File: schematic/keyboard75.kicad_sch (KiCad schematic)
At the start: 389 parts, among them J1 SWD, J1 USB_C_Receptacle_USB2.0, J4 PTH, J5 PTH, K0_0 KEYSW, K0_1 KEYSW, K0_10 KEYSW, K0_11 KEYSW, K0_12 KEYSW, K0_13 KEYSW, K0_14 KEYSW, K0_15 KEYSW, K0_2 KEYSW, K0_3 KEYSW, K0_4 KEYSW, K0_5 KEYSW, K0_6 KEYSW, K0_7 KEYSW, K0_8 KEYSW, K0_9 KEYSW, K1_0 KEYSW, K1_1 KEYSW, K1_10 KEYSW, K1_11 KEYSW, K1_12 KEYSW, K1_13 KEYSW, K1_14 KEYSW, K1_2 KEYSW, K1_3 KEYSW, K1_4 KEYSW, K1_5 KEYSW, K1_6 KEYSW, K1_7 KEYSW, K1_8 KEYSW, K1_9 KEYSW, K2_0 KEYSW, K2_1 KEYSW, K2_10 KEYSW, K2_11 KEYSW, K2_12 KEYSW, K2_13 KEYSW, K2_14 KEYSW, K2_2 KEYSW, K2_3 KEYSW, K2_4 KEYSW, K2_5 KEYSW, K2_6 KEYSW, K2_7 KEYSW, K2_8 KEYSW, K2_9 KEYSW, K3_0 KEYSW, K3_1 KEYSW, K3_10 KEYSW, K3_11 KEYSW, K3_12 KEYSW, K3_13 KEYSW, K3_2 KEYSW, K3_3 KEYSW, K3_4 KEYSW, K3_5 KEYSW, K3_6 KEYSW, K3_7 KEYSW, K3_8 KEYSW, K3_9 KEYSW, K4_0 KEYSW, K4_1 KEYSW, K4_10 KEYSW, K4_11 KEYSW, K4_12 KEYSW, K4_13 KEYSW, K4_14 KEYSW, K4_2 KEYSW, K4_3 KEYSW, K4_4 KEYSW, K4_5 KEYSW, K4_6 KEYSW, K4_7 KEYSW, K4_8 KEYSW, K4_9 KEYSW, K5_0 KEYSW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

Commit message: PCB traces added
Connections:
- net BAT_VOLT: now also U6.10 (P0.30/AIN6); no longer U6.9 (P0.31/AIN7)
- net CHARGE_CTRL_2: now also U6.9 (P0.31/AIN7); no longer U6.10 (P0.30/AIN6)
- net col0: now also U6.22 (P0.07); no longer U6.36 (P1.00)
- net col1: now also U6.20 (P0.12); no longer U6.12 (P0.26)
- net col10: now also U6.32 (P0.20); no longer U6.38 (P1.02)
- net col11: now also U6.34 (P0.22); no longer U6.16 (P0.08)
- net col12: now also U6.36 (P1.00); no longer U6.22 (P0.07)
- net col13: now also U6.38 (P1.02); no longer U6.14 (P0.06)
- net col14: now also U6.33 (P0.13); no longer U6.15 (P0.05/AIN3)
- net col15: now also U6.35 (P0.24); no longer U6.18 (P0.04/AIN2)
- net col2: now also U6.18 (P0.04/AIN2); no longer U6.35 (P0.24)
- net col3: now also U6.16 (P0.08); no longer U6.34 (P0.22)
- net col4: now also U6.14 (P0.06); no longer U6.32 (P0.20)
- net col5: now also U6.12 (P0.26); no longer U6.30 (P0.17)
- net col6: now also U6.42 (P1.06); no longer U6.28 (P0.15)
- net col7: now also U6.40 (P1.04); no longer U6.33 (P0.13)
- net col8: now also U6.28 (P0.15); no longer U6.20 (P0.12)
- net col9: now also U6.30 (P0.17); no longer U6.40 (P1.04)

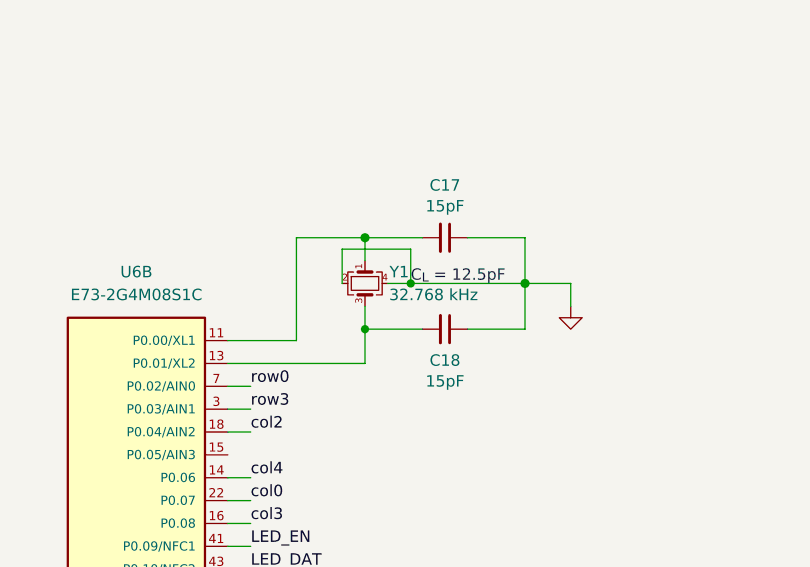
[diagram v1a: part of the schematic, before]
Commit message: added ZMK config
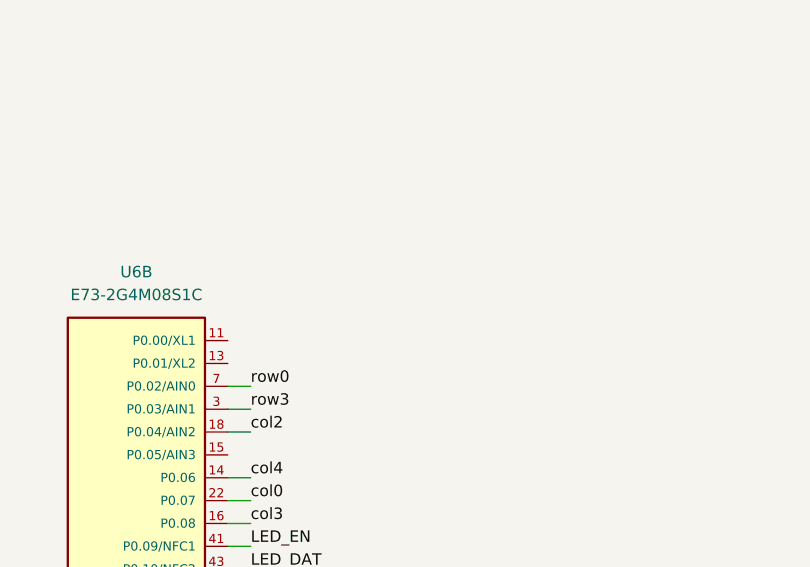
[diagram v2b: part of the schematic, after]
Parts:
- removed C17, C18: 15pF, Capacitor_SMD:C_0402_1005Metric, symbol Device:C_Small
- removed Y1: 32.768 kHz, Crystal:Crystal_SMD_2016-4Pin_2.0x1.6mm, symbol Device:Crystal_GND24_Small
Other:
- note removed: "C_{L} = 12.5pF"
